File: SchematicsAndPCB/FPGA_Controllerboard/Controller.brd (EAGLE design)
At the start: 100 x 80 mm, 71 parts, among them J5 DCJ0202, T1 BC237, T10 BC237, T11 BC237, T12 BC237, T13 BC237, T14 BC237, T17 BC237, T18 BC237, T2 BC237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

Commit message: update on PCB
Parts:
- removed LD1117: 22-23-2031, con-molex:22-23-2031
- added IC1: LM1117T-3.3-V, lm1117:TO220V
- moved C2 11.1 mm to (90.9, 19.8)
- moved C1 7.41 mm to (70.6, 14.5), turned to 180 degrees
- moved C3 7.12 mm to (72.4, 8.38), turned to 180 degrees
- moved LED2 3.97 mm to (65.8, 8.89)
- moved R31 1.55 mm to (63.5, 2.29)
- renumbered SV1 to SENSORIN, SV2(MOTOR_DRIVER) to MOTOR_DRIVER, SV3(SEVENSEG) to SEVENSEG, SV4(FLOORBUTTON) to FLOORBUTTON, SV5(MENUBUTTON)1 to MENUBUTTON
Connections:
- net GND: now also IC1.1; no longer LD1117.3
- net MOTORVCC: now also IC1.3; no longer LD1117.1
- net VCC: now also IC1.2; no longer LD1117.2
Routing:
- net MOTORVCC: track 84.1 -> 28.9 mm
- net VCC: track 231.1 -> 202.8 mm
- net N$41: track 5.16 -> 7.24 mm
- net GND: track 345.3 -> 346.1 mm, vias 0 -> 182
- net N$37: track 5.26 -> 5.82 mm
- removed copper zone on layer 16, net N$18
- removed copper zone on layer 1, net VCC

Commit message: update
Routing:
- net SOFTRST: track 26.0 -> 24.8 mm
- net SLEEP_GENERATED: track 10.2 -> 10.8 mm
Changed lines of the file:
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@@
 <?xml version="1.0" encoding="utf-8"?>
 <!DOCTYPE eagle SYSTEM "eagle.dtd">
-<eagle version="7.2.0">
+<eagle version="7.3.0">
 <drawing>
 <settings>
@@
 <contactref element="J1" pad="10"/>
 <contactref element="J4" pad="17"/>
-<wire x1="53.34" y1="54.61" x2="57.15" y2="54.61" width="0.4064" layer="1"/>
-<wire x1="57.15" y1="54.61" x2="58.928" y2="52.832" width="0.4064" layer="1"/>
-<wire x1="58.928" y1="52.832" x2="58.928" y2="38.354" width="0.4064" layer="1"/>
-<wire x1="58.928" y1="38.354" x2="60.452" y2="36.83" width="0.4064" layer="1"/>
-<wire x1="60.452" y1="36.83" x2="63.5" y2="36.83" width="0.4064" layer="1"/>
+<wire x1="53.34" y1="54.61" x2="55.118" y2="54.61" width="0.8128" layer="16"/>
+<wire x1="55.118" y1="54.61" x2="58.42" y2="51.308" width="0.8128" layer="16"/>
+<wire x1="58.42" y1="51.308" x2="58.42" y2="38.862" width="0.8128" layer="16"/>
+<wire x1="58.42" y1="38.862" x2="60.452" y2="36.83" width="0.8128" layer="16"/>
+<wire x1="60.452" y1="36.83" x2="63.5" y2="36.83" width="0.8128" layer="16"/>
 </signal>
 <signal name="MCLK_GENERATED">
 <contactref element="J1" pad="18"/>
 <contactref element="J4" pad="18"/>
-<wire x1="53.34" y1="34.29" x2="63.5" y2="34.29" width="0.4064" layer="16"/>
+<wire x1="53.34" y1="34.29" x2="63.5" y2="34.29" width="0.8128" layer="16"/>
 </signal>
 <signal name="DIR_GENERATED">
 <contactref element="J1" pad="19"/>
 <contactref element="J4" pad="19"/>
-<wire x1="63.5" y1="31.75" x2="53.34" y2="31.75" width="0.4064" layer="16"/>
+<wire x1="63.5" y1="31.75" x2="53.34" y2="31.75" width="0.8128" layer="16"/>
 </signal>
 <signal name="SLEEP_GENERATED">
 <contactref element="J1" pad="20"/>
 <contactref element="J4" pad="20"/>
-<wire x1="53.34" y1="29.21" x2="63.5" y2="29.21" width="0.4064" layer="16"/>
+<wire x1="53.34" y1="29.21" x2="63.754" y2="29.21" width="0.8128" layer="16"/>
+<wire x1="63.754" y1="29.21" x2="64.008" y2="29.464" width="0.8128" layer="16"/>
+<wire x1="64.008" y1="29.464" x2="63.5" y2="29.21" width="0" layer="19" extent="1-16"/>
 </signal>
 <signal name="N$3">

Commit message: Update
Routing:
- net N$15: track 15.5 -> 21.7 mm
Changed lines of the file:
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@@
 <?xml version="1.0" encoding="utf-8"?>
 <!DOCTYPE eagle SYSTEM "eagle.dtd">
-<eagle version="7.3.0">
+<eagle version="7.2.0">
 <drawing>
 <settings>
@@
 <contactref element="J4" pad="10"/>
 <wire x1="27.686" y1="54.61" x2="30.48" y2="54.61" width="0.8128" layer="16"/>
-<wire x1="27.686" y1="54.61" x2="49.784" y2="54.61" width="0.4064" layer="1"/>
+<wire x1="27.686" y1="54.61" x2="49.784" y2="54.61" width="0.8128" layer="1"/>
 <wire x1="49.784" y1="54.61" x2="51.054" y2="55.88" width="0.4064" layer="1"/>
 <wire x1="51.054" y1="55.88" x2="62.23" y2="55.88" width="0.4064" layer="1"/>
@@
 <wire x1="19.812" y1="58.42" x2="26.416" y2="58.42" width="0.4064" layer="1"/>
 <wire x1="26.416" y1="58.42" x2="27.686" y2="57.15" width="0.4064" layer="1"/>
-<wire x1="30.48" y1="57.15" x2="49.276" y2="57.15" width="0.4064" layer="1"/>
+<wire x1="30.48" y1="57.15" x2="49.276" y2="57.15" width="0.8128" layer="1"/>
 <wire x1="49.276" y1="57.15" x2="50.546" y2="58.42" width="0.4064" layer="1"/>
 <wire x1="50.546" y1="58.42" x2="62.23" y2="58.42" width="0.4064" layer="1"/>
@@
 <contactref element="J2" pad="8"/>
 <contactref element="J4" pad="8"/>
-<wire x1="30.48" y1="59.69" x2="49.784" y2="59.69" width="0.4064" layer="1"/>
+<wire x1="30.48" y1="59.69" x2="49.784" y2="59.69" width="0.8128" layer="1"/>
 <wire x1="49.784" y1="59.69" x2="51.054" y2="60.96" width="0.4064" layer="1"/>
 <wire x1="51.054" y1="60.96" x2="62.23" y2="60.96" width="0.4064" layer="1"/>
@@
 <contactref element="J2" pad="7"/>
 <contactref element="J4" pad="7"/>
-<wire x1="30.48" y1="62.23" x2="50.038" y2="62.23" width="0.4064" layer="1"/>
+<wire x1="30.48" y1="62.23" x2="50.038" y2="62.23" width="0.8128" layer="1"/>
 <wire x1="50.038" y1="62.23" x2="51.308" y2="63.5" width="0.4064" layer="1"/>
 <wire x1="51.308" y1="63.5" x2="62.23" y2="63.5" width="0.4064" layer="1"/>
@@
 <contactref element="J2" pad="6"/>
 <contactref element="J4" pad="6"/>
-<wire x1="30.48" y1="64.77" x2="50.292" y2="64.77" width="0.4064" layer="1"/>
+<wire x1="30.48" y1="64.77" x2="50.292" y2="64.77" width="0.8128" layer="1"/>
 <wire x1="50.292" y1="64.77" x2="51.562" y2="66.04" width="0.4064" layer="1"/>
 <wire x1="51.562" y1="66.04" x2="62.23" y2="66.04" width="0.4064" layer="1"/>
@@
 <contactref element="J2" pad="5"/>
 <contactref element="J4" pad="5"/>
-<wire x1="30.48" y1="67.31" x2="49.784" y2="67.31" width="0.4064" layer="1"/>
+<wire x1="30.48" y1="67.31" x2="49.784" y2="67.31" width="0.8128" layer="1"/>
 <wire x1="49.784" y1="67.31" x2="51.054" y2="68.58" width="0.4064" layer="1"/>
 <wire x1="51.054" y1="68.58" x2="55.626" y2="68.58" width="0.4064" layer="1"/>
@@
 <contactref element="J2" pad="4"/>
 <contactref element="J4" pad="4"/>
-<wire x1="30.48" y1="69.85" x2="49.784" y2="69.85" width="0.4064" layer="1"/>
+<wire x1="30.48" y1="69.85" x2="49.784" y2="69.85" width="0.8128" layer="1"/>
 <wire x1="49.784" y1="69.85" x2="51.054" y2="71.12" width="0.4064" layer="1"/>
 <wire x1="51.054" y1="71.12" x2="62.23" y2="71.12" width="0.4064" layer="1"/>
@@
 <contactref element="S6" pad="1"/>
 <contactref element="J5" pad="1"/>
-<wire x1="85.8" y1="5.08" x2="88.138" y2="5.08" width="0.8128" layer="16"/>
-<wire x1="88.138" y1="5.08" x2="96.52" y2="13.462" width="0.8128" layer="16"/>
-<wire x1="96.52" y1="13.462" x2="96.52" y2="14.732" width="0.8128" layer="16"/>
+<wire x1="85.8" y1="5.08" x2="85.8" y2="6.148" width="0.8128" layer="16"/>
+<wire x1="85.8" y1="6.148" x2="83.82" y2="8.128" width="0.8128" layer="16"/>
+<wire x1="83.82" y1="8.128" x2="83.82" y2="10.668" width="0.8128" layer="16"/>
+<wire x1="83.82" y1="10.668" x2="85.598" y2="12.446" width="0.8128" layer="16"/>
+<wire x1="85.598" y1="12.446" x2="95.758" y2="12.446" width="0.8128" layer="16"/>
+<wire x1="95.758" y1="12.446" x2="96.52" y2="13.208" width="0.8128" layer="16"/>
+<wire x1="96.52" y1="13.208" x2="96.52" y2="14.732" width="0.8128" layer="16"/>
 </signal>
 <signal name="N$16">
@@
 <wire x1="86.36" y1="72.39" x2="66.802" y2="72.39" width="0.4064" layer="16"/>
 <wire x1="66.802" y1="72.39" x2="65.532" y2="73.66" width="0.4064" layer="16"/>
-<wire x1="65.532" y1="73.66" x2="55.88" y2="73.66" width="0.4064" layer="16"/>
+<wire x1="65.532" y1="73.66" x2="55.88" y2="73.66" width="0.6096" layer="16"/>
 <wire x1="55.88" y1="73.66" x2="54.61" y2="72.39" width="0.4064" layer="16"/>
 <wire x1="54.61" y1="72.39" x2="53.34" y2="72.39" width="0.4064" layer="16"/>

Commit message: FPGA PCB update
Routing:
- net SO1: track 57.3 -> 54.6 mm
- net GND: track 346.1 -> 345.3 mm, vias 182 -> 463

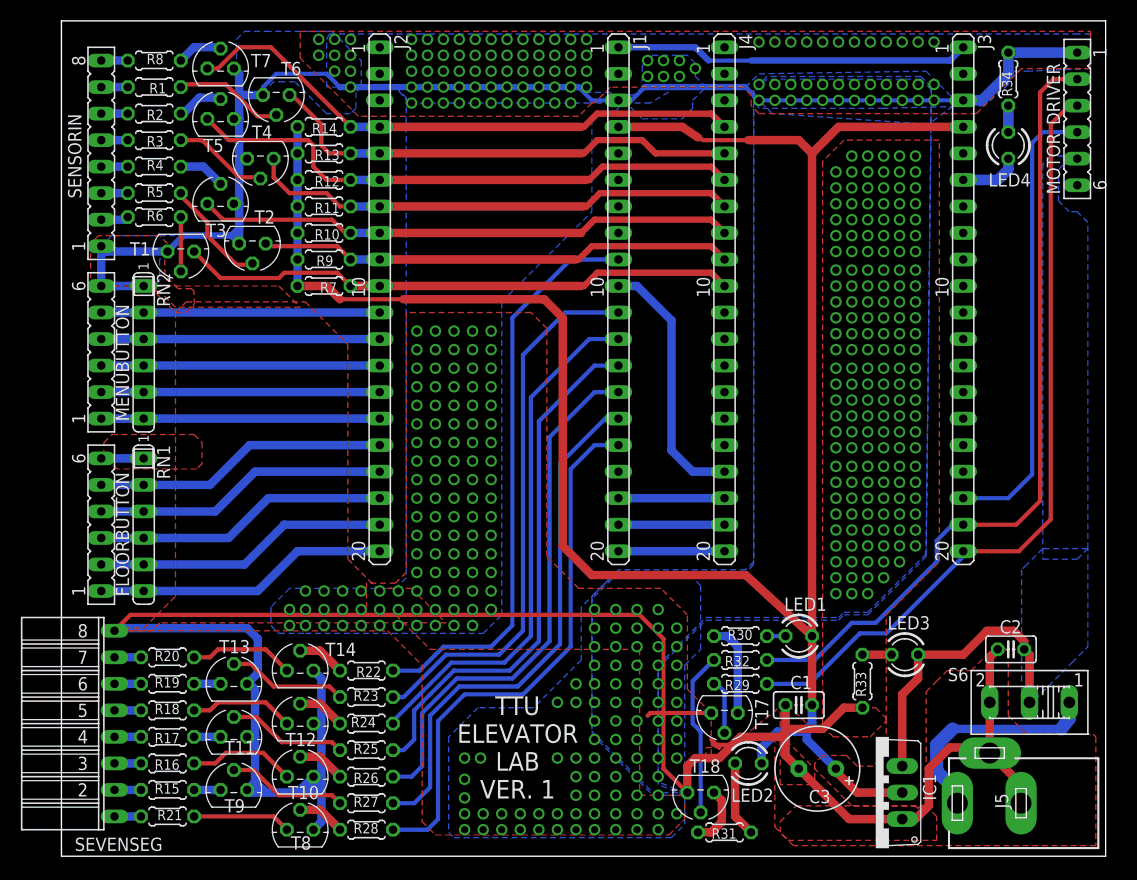
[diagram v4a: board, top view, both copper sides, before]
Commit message: additional vcc/gnd + holes + heatsink
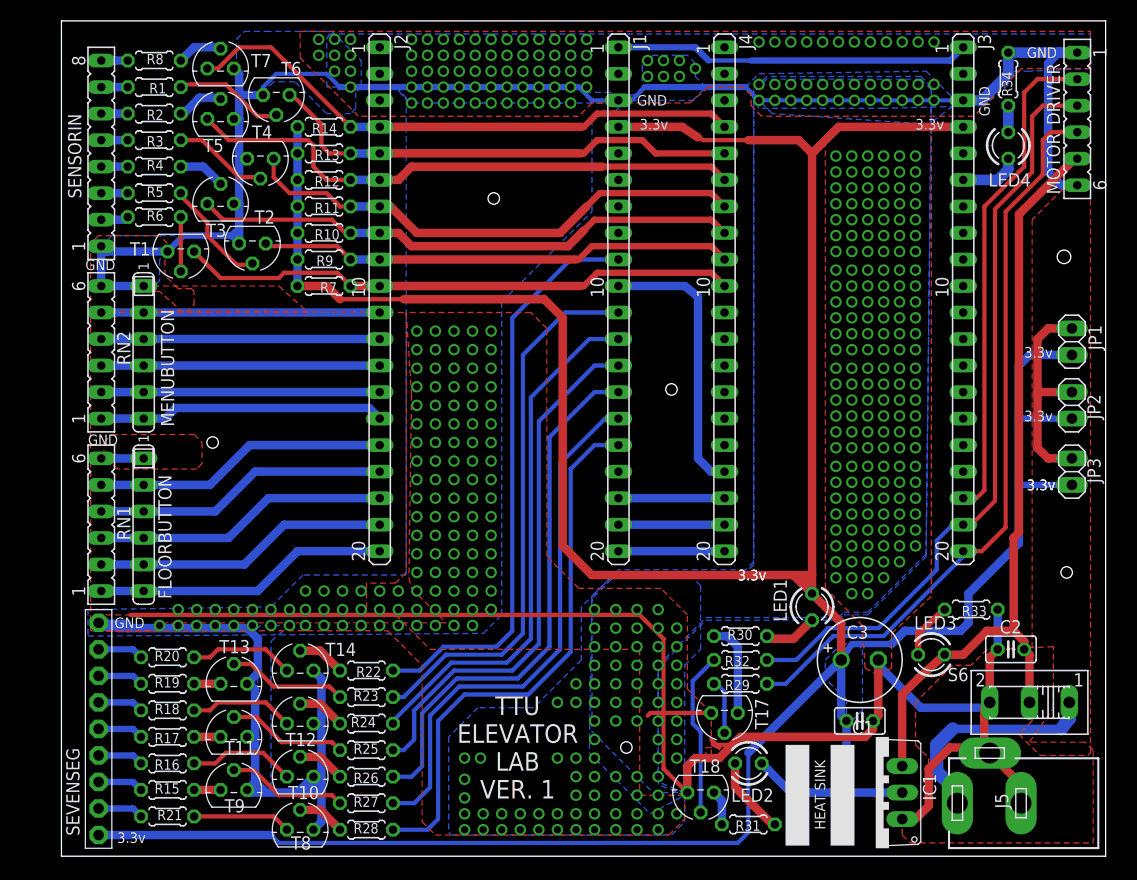
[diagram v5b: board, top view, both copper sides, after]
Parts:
- added JP1, JP2, JP3: (no value), pinhead:1X02
- SEVENSEG: device con-lsta:FE08W -> adafruit:1X09-BIG
- moved R33 12.5 mm to (87.1, 23.6), turned to 180 degrees
- moved C3 11.2 mm to (76.5, 18.8), turned to 0 degrees
- moved C1 6.04 mm to (76.5, 13.0), turned to 0 degrees
- moved LED1 3.07 mm to (71.9, 23.9), turned to 270 degrees
- moved LED3 2.54 mm to (83.3, 19.3)
- moved R31 2.41 mm to (65.8, 3.05)
- moved SEVENSEG 1.61 mm to (3.56, 12.2)
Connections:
- net DIR: now also MOTOR_DRIVER.3; no longer MOTOR_DRIVER.2
- net GND: now also JP1.2, JP2.2, JP3.2, MOTOR_DRIVER.6, SEVENSEG.9; no longer SEVENSEG.8
- net MOTORCLK: now also MOTOR_DRIVER.2; no longer MOTOR_DRIVER.4
- net ON_BOARDSS1: now also SEVENSEG.2; no longer SEVENSEG.1
- net ON_BOARDSS2: now also SEVENSEG.3; no longer SEVENSEG.2
- net ON_BOARDSS3: now also SEVENSEG.4; no longer SEVENSEG.3
- net ON_BOARDSS4: now also SEVENSEG.5; no longer SEVENSEG.4
- net ON_BOARDSS5: now also SEVENSEG.6; no longer SEVENSEG.5
- net ON_BOARDSS6: now also SEVENSEG.7; no longer SEVENSEG.6
- net ON_BOARDSS7: now also SEVENSEG.8; no longer SEVENSEG.7
- net SLEEP: now also MOTOR_DRIVER.4; no longer MOTOR_DRIVER.3
- net VCC: now also JP1.1, JP2.1, JP3.1, SEVENSEG.1
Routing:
- net VCC: track 202.8 -> 344.0 mm
- net MOTORVCC: track 28.9 -> 75.7 mm
- net GND: track 345.3 -> 390.3 mm, vias 463 -> 472
- net DIR: track 77.6 -> 72.8 mm
- net MOTORCLK: track 44.0 -> 47.6 mm
- net SLEEP: track 75.1 -> 71.5 mm
- net N$40: track 1.78 -> 5.16 mm
- net N$39: track 2.79 -> 5.45 mm
- net N$37: track 5.82 -> 3.36 mm
- net SO4: track 47.2 -> 49.3 mm
- net ON_BOARDSS7: track 2.54 -> 4.38 mm
- net ON_BOARDSS4: track 2.54 -> 4.38 mm
- net ON_BOARDSS2: track 2.54 -> 4.38 mm
- net ON_BOARDSS1: track 2.54 -> 4.38 mm
- net ON_BOARDSS5: track 2.54 -> 4.38 mm
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- added copper zone on layer 16, net VCC
- removed copper zone on layer 16, net MOTORVCC
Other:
- board text added: "3.3v"
- board text added: "GND"
- board text added: "HEAT SINK"

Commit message: getting ready for printing
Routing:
- net VCC: track 344.0 -> 334.3 mm
- net N$15: track 21.8 -> 25.6 mm
- net GND: track 390.3 -> 392.1 mm, vias 472 -> 458
